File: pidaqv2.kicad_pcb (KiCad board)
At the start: 2 copper layers, 66 x 66 mm, 18 parts, among them P1 Conn_02x20_Odd_Even, U1 INA2126E_250, U2 ADS114S08BIPBS, U3 ADS114S08BIPBS

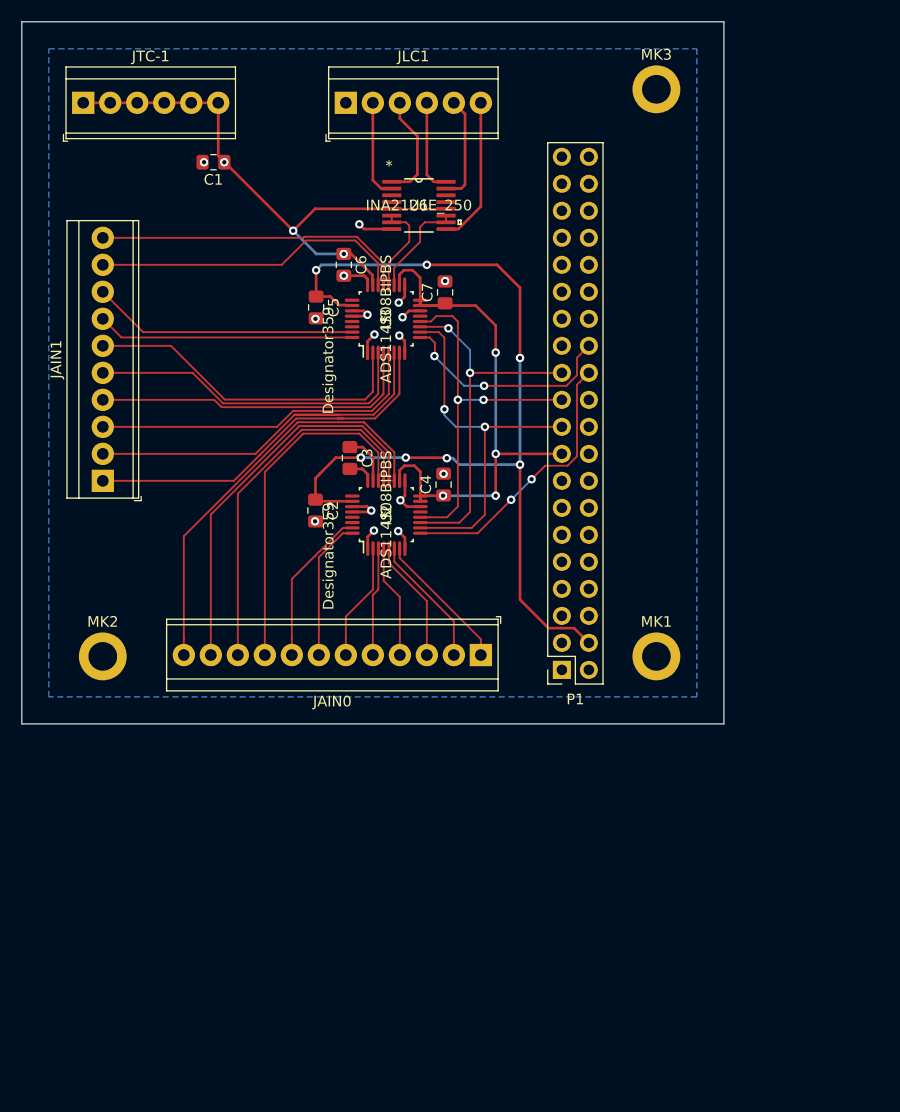
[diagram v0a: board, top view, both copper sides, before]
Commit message: silkscreen added
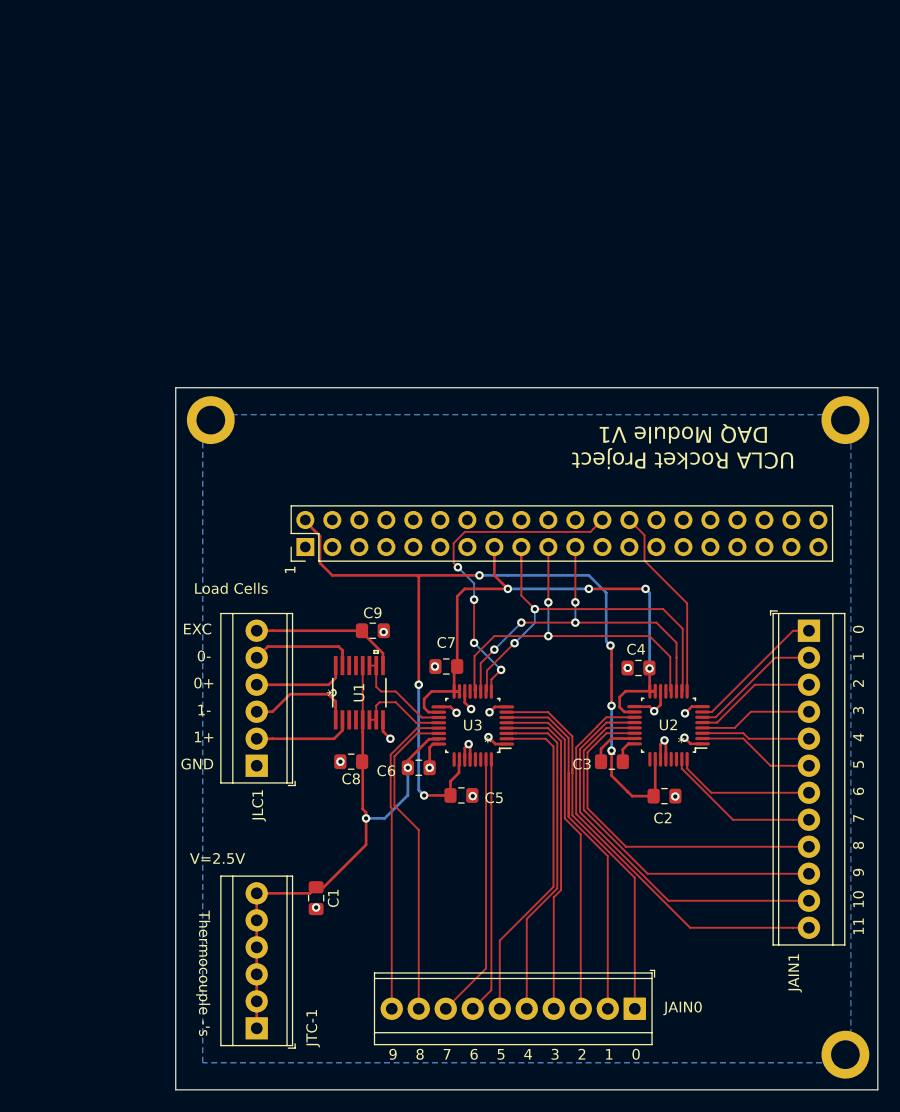
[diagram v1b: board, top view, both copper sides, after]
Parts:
- removed P1: Conn_02x20_Odd_Even, Connector_PinSocket_2.54mm:PinSocket_2x20_P2.54mm_Vertical
- added C8: 0.1uF, Capacitor_SMD:C_0805_2012Metric_Pad1.15x1.40mm_HandSolder, F.Cu at (119.9, 130.6)
- added C9: 0.1uF, Capacitor_SMD:C_0805_2012Metric_Pad1.15x1.40mm_HandSolder, F.Cu at (121.9, 118.2)
- added J1: Raspberry_Pi_2_3, Connector_PinHeader_2.54mm:PinHeader_2x20_P2.54mm_Vertical, F.Cu at (115.6, 110.4)
- moved JTC-1 88.6 mm to (111.0, 155.6), turned to 90 degrees
- moved MK2 79.3 mm to (166.4, 158.1), turned to 90 degrees
- moved JAIN0 70.5 mm to (146.6, 153.8), turned to 180 degrees
- moved C1 69.9 mm to (116.6, 143.4), turned to 270 degrees
- moved JLC1 62.9 mm to (111.0, 130.9), turned to 90 degrees
- moved MK3 52.2 mm to (106.7, 98.4), turned to 90 degrees
- moved C5 47.9 mm to (130.2, 133.7), turned to 0 degrees
- moved C6 47.8 mm to (126.2, 131.1), turned to 0 degrees
- moved U1 46.2 mm to (120.7, 124.1), turned to 90 degrees
- moved C2 42.4 mm to (149.4, 133.8), turned to 0 degrees
- moved U3 39.1 mm to (131.3, 127.1), turned to 180 degrees
- moved C3 37.7 mm to (144.4, 130.6), turned to 0 degrees
- moved C7 35.2 mm to (128.8, 121.6), turned to 180 degrees
- moved U2 33.1 mm to (149.7, 127.1), turned to 180 degrees
- moved JAIN1 30.9 mm to (162.9, 118.2), turned to 270 degrees
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- renumbered JAIN1 to JAIN0, JAIN0 to JAIN1
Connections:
- net /MISO renamed MISO
- net /MOSI renamed MOSI
- net /SCLK renamed SCLK
- U2 pad 9: /CE0 -> ~CE1
- U3 pad 9: /CE1 -> ~CE0
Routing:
- net ~CE0: track 0.00 -> 31.1 mm, vias 0 -> 4
- net /CE0: track 26.0 -> 0.00 mm, vias 2 -> 0
- net /CE1: track 21.1 -> 0.00 mm, vias 2 -> 0
- net ~CE1: track 0.00 -> 18.4 mm
- net +5V: track 89.9 -> 85.7 mm, vias 7 -> 6
- net MOSI: track 36.1 -> 37.7 mm
- net +3V3: track 52.7 -> 54.1 mm
- net GND: track 31.1 -> 30.0 mm, vias 16 -> 18
- net +2.5V: track 53.1 -> 53.8 mm, vias 3 -> 2
- net SCLK: track 34.6 -> 35.0 mm, vias 2 -> 4
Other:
- board text added: "0"
- board text added: "0+"
- board text added: "0-"
- board text added: "1"
- board text added: "1+"
- board text added: "1-"
- board text added: "10"
- board text added: "11"
- board text added: "2"
- board text added: "3"
- board text added: "4"
- board text added: "5"
- board text added: "6"
- board text added: "7"
- board text added: "8"
- board text added: "9"
- board text added: "EXC"
- board text added: "GND"
- board text added: "Load Cells"
- board text added: "Thermocouple -'s"
- board text added: "UCLA Rocket Project DAQ Module V1"
- board text added: "V=2.5V"

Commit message: redid SPI traces
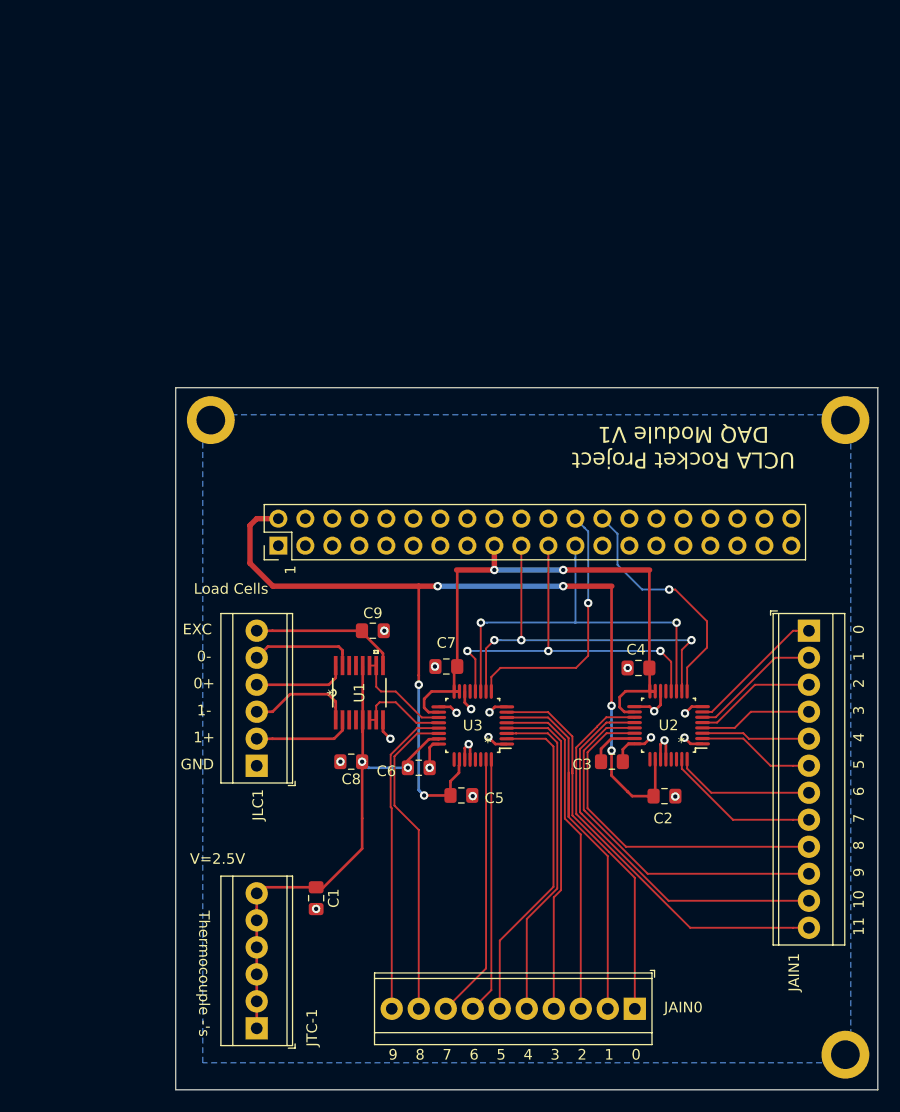
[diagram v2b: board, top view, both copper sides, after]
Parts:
- moved J1 2.54 mm to (113.0, 110.2)
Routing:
- net +5V: track 85.7 -> 93.6 mm
- net ~CE0: track 31.1 -> 24.7 mm, vias 4 -> 1
- net ~CE1: track 18.4 -> 22.9 mm, vias 0 -> 1
- net SCLK: track 35.0 -> 38.6 mm, vias 4 -> 2
- net +3V3: track 54.1 -> 56.3 mm, vias 4 -> 2
- net +2.5V: track 53.8 -> 51.8 mm
- net GND: track 30.0 -> 31.8 mm, vias 18 -> 19
- net MISO: track 34.9 -> 36.4 mm, vias 2 -> 3
- net MOSI: track 37.7 -> 38.4 mm, vias 2 -> 3
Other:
- rule via_min_size: 0.4 -> 0.3048
